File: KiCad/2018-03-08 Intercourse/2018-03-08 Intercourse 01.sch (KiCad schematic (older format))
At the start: 27 parts

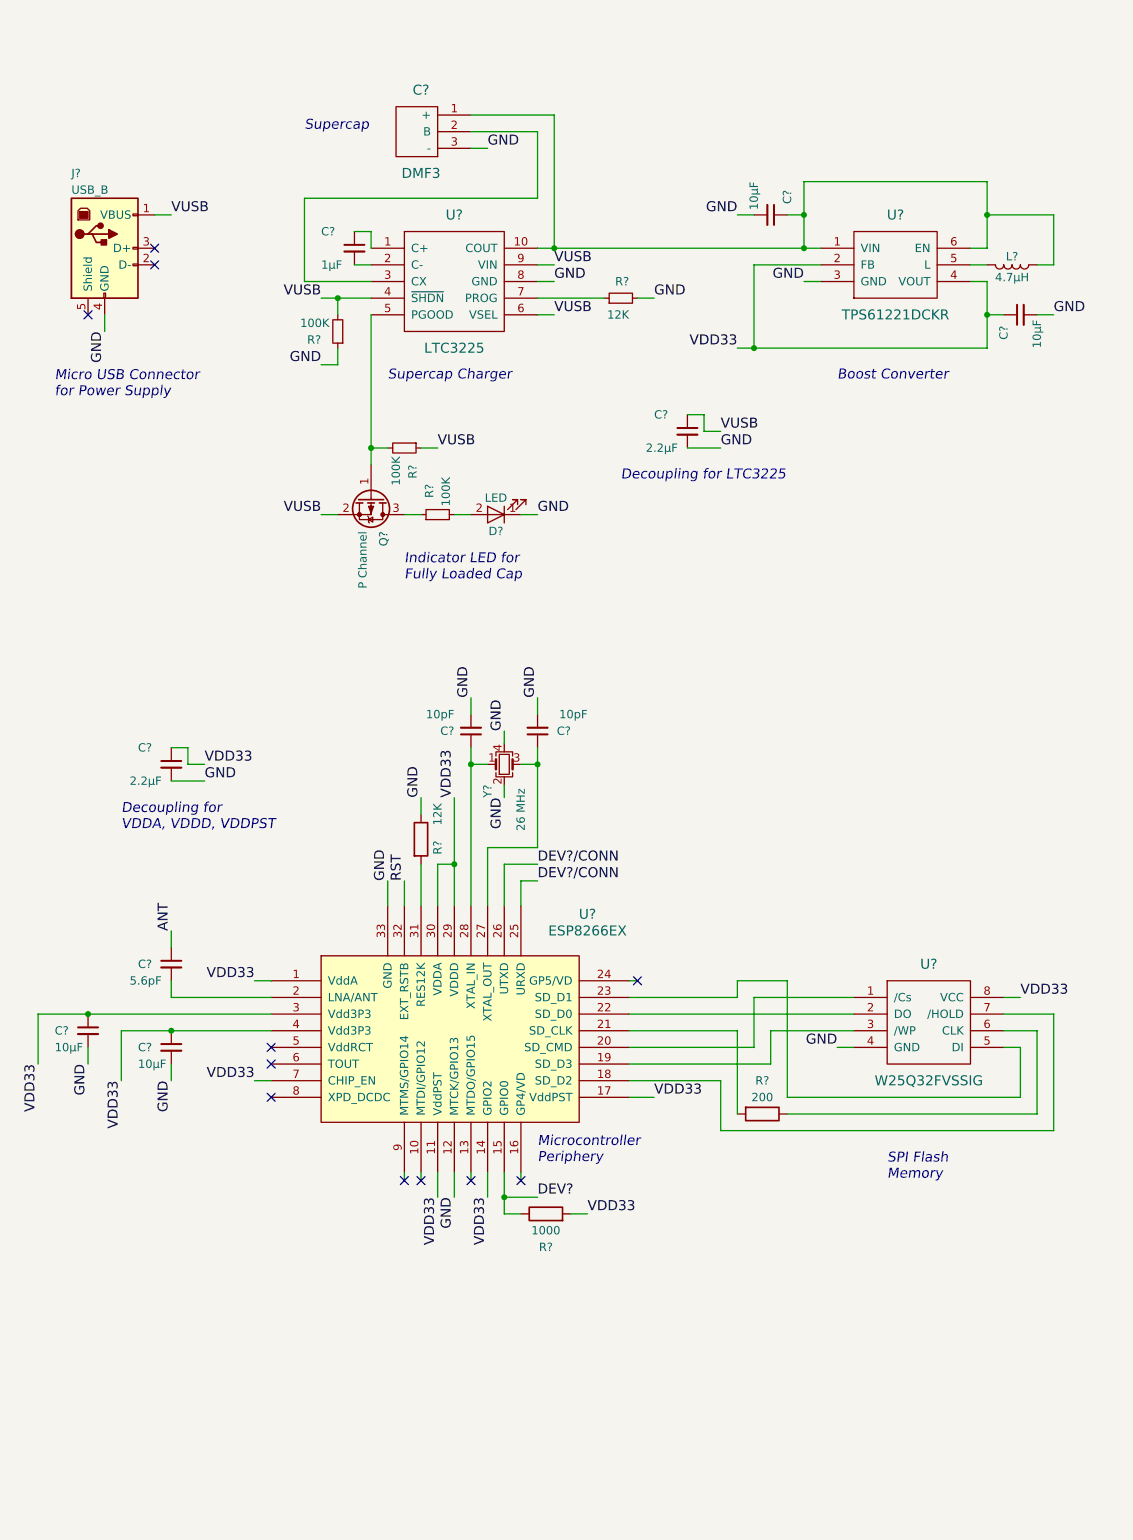
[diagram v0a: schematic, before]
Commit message: clean up schematic
* added connector
* changed labels
* made some stuff cleaner
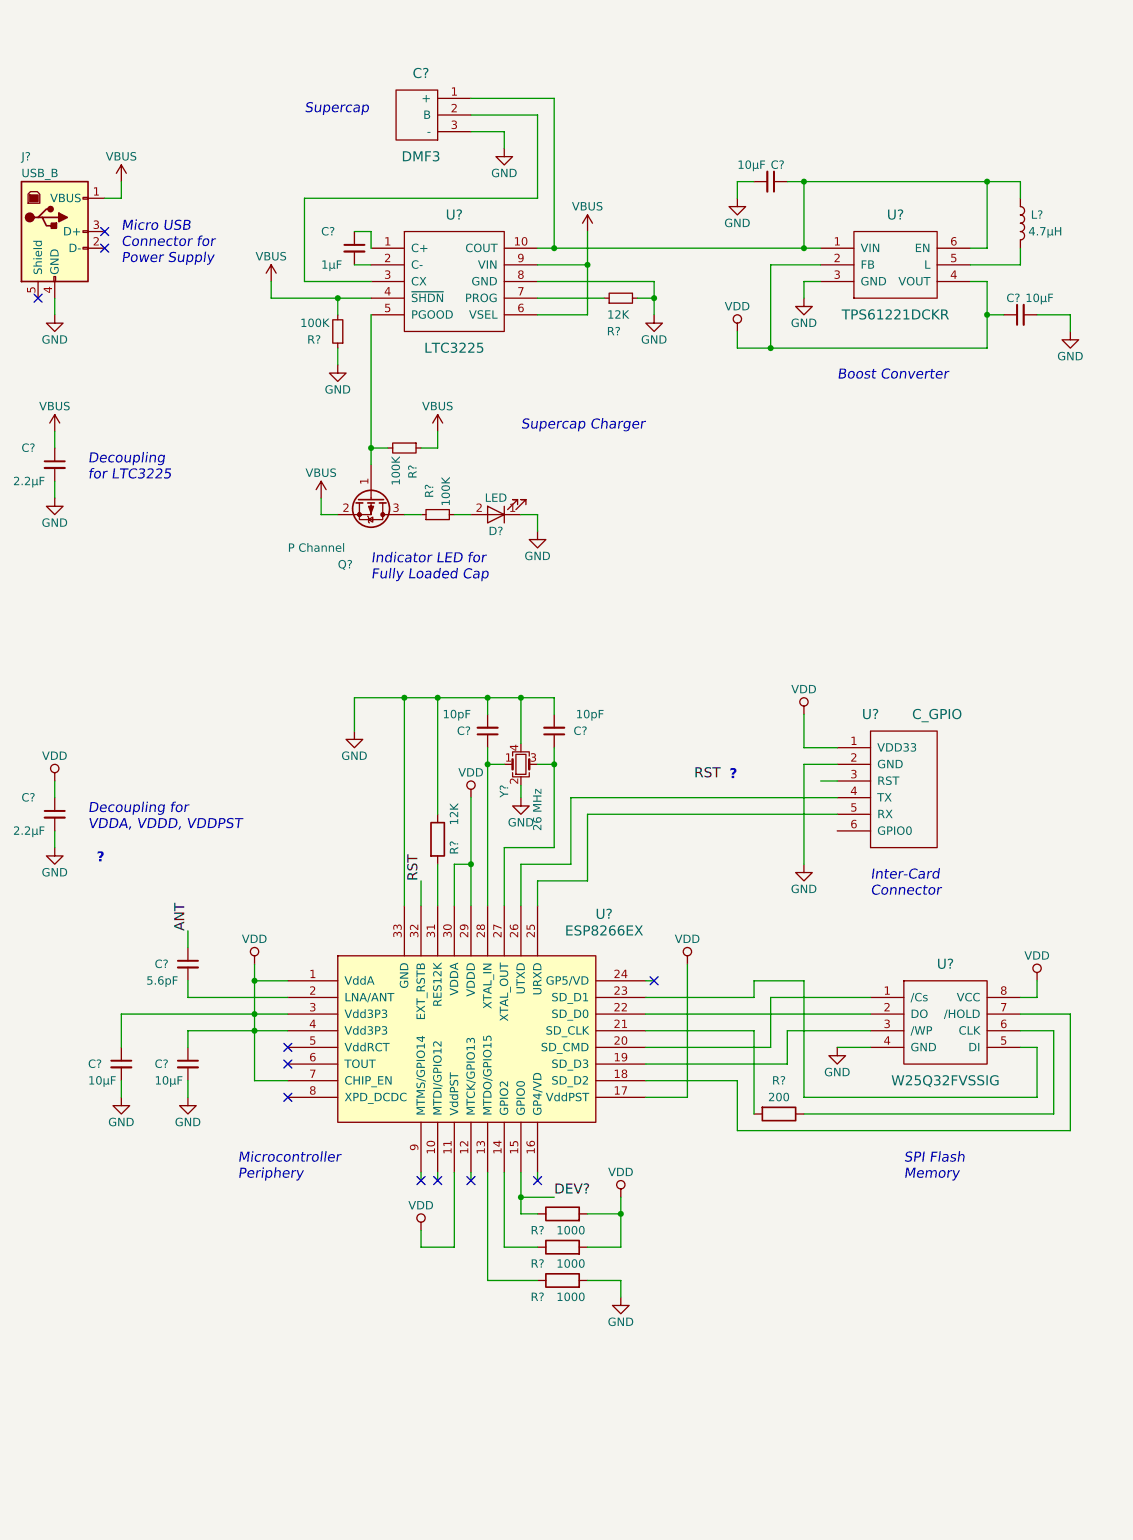
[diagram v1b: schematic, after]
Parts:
- added R? (x2): 1000, symbol R
- added U?: C_GPIO, symbol C_GPIO
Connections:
- net GND: now also R?.2, U?.2 (GND); no longer U?.12 (MTCK/GPIO13)
- net at U?.13 (MTDO/GPIO15): now also R?.1
- net DEV?/CONN: no longer names the net of U?.25 (URXD)
- net DEV?/CONN: now also U?.5 (RX); no longer U?.26 (UTXD)
- net VDD33 renamed VDD
- net VDD: now also R?.2, U?.1 (VDD33); no longer U?.14 (GPIO2)
- net VUSB renamed VBUS
- new net: R?.1, U?.14 (GPIO2)
- new net: U?.26 (UTXD), U?.4 (TX)
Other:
- note added: "?"
- note added: "Decoupling\nfor LTC3225"
- note added: "Inter-Card\nConnector"
- note added: "Micro USB\nConnector for\nPower Supply"
- note removed: "Decoupling for LTC3225"
- note removed: "Micro USB Connector\nfor Power Supply"
- moved on the sheet: C?, J?, L?, R?, U?, Y?

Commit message: further cleaning
* cleaned up
* added todos
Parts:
- added AE?: Antenna, symbol Antenna
- added C?: 1μF, symbol C_Small
- added R?: 10K, symbol R
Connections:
- net DEV? is gone; now on net FLASH: R?.1, U?.15 (GPIO0)
- net RST: now also U?.3 (RST), C?.1, R?.2
- net VDD: now also R?.1
- net FLASH: now reaches U?.6 (GPIO0)
- net ANT: no longer names the net of C?.1
- net ANT: now also AE?.1 (A)
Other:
- note added: "Todo:\n* Status LEDs\n* USB Conn Check\n* Reset"
- moved on the sheet: C?, R?, U?

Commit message: changes labels
Because I like them better ...
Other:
- moved on the sheet: R?
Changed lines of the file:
@@
 L R R?
 U 1 1 5AADBBEB
-P 4150 8200
-F 0 "R?" V 4050 8350 50  0000 C CNN
-F 1 "1000" V 4050 8150 50  0000 C CNN
-F 2 "" V 4080 8200 50  0001 C CNN
-F 3 "" H 4150 8200 50  0001 C CNN
-	1    4150 8200
+P 4150 8300
+F 0 "R?" V 4050 8450 50  0000 C CNN
+F 1 "1000" V 4050 8250 50  0000 C CNN
+F 2 "" V 4080 8300 50  0001 C CNN
+F 3 "" H 4150 8300 50  0001 C CNN
+	1    4150 8300
 	0    -1   -1   0
 $EndComp
-Text Label 4100 8100 0    60   ~ 0
-FLASH
-Text Label 3300 6200 1    60   ~ 0
-RST
 NoConn ~ 2500 7500
 NoConn ~ 2500 7300
@@
 Text Notes 6000 6300 0    60   Italic 0
 Inter-Card\nConnector
-Text Label 5100 5600 2    60   ~ 0
-RST
 $Comp
 L C_GPIO U?
@@
 L R R?
 U 1 1 5AB011DC
-P 4150 8400
-F 0 "R?" V 4050 8550 50  0000 C CNN
-F 1 "1000" V 4050 8350 50  0000 C CNN
-F 2 "" V 4080 8400 50  0001 C CNN
-F 3 "" H 4150 8400 50  0001 C CNN
-	1    4150 8400
+P 4150 8500
+F 0 "R?" V 4050 8650 50  0000 C CNN
+F 1 "1000" V 4050 8450 50  0000 C CNN
+F 2 "" V 4080 8500 50  0001 C CNN
+F 3 "" H 4150 8500 50  0001 C CNN
+	1    4150 8500
 	0    -1   -1   0
 $EndComp
@@
 L R R?
 U 1 1 5AB01E0B
-P 4150 8600
-F 0 "R?" V 4050 8750 50  0000 C CNN
-F 1 "1000" V 4050 8550 50  0000 C CNN
-F 2 "" V 4080 8600 50  0001 C CNN
-F 3 "" H 4150 8600 50  0001 C CNN
-	1    4150 8600
+P 4150 8700
+F 0 "R?" V 4050 8850 50  0000 C CNN
+F 1 "1000" V 4050 8650 50  0000 C CNN
+F 2 "" V 4080 8700 50  0001 C CNN
+F 3 "" H 4150 8700 50  0001 C CNN
+	1    4150 8700
 	0    -1   -1   0
 $EndComp
@@
 L GND #PWR?
 U 1 1 5AB02ABD
-P 4500 8700
-F 0 "#PWR?" H 4500 8450 50  0001 C CNN
-F 1 "GND" H 4500 8550 50  0000 C CNN
-F 2 "" H 4500 8700 50  0001 C CNN
-F 3 "" H 4500 8700 50  0001 C CNN
-	1    4500 8700
+P 4600 8800
+F 0 "#PWR?" H 4600 8550 50  0001 C CNN
+F 1 "GND" H 4600 8650 50  0000 C CNN
+F 2 "" H 4600 8800 50  0001 C CNN
+F 3 "" H 4600 8800 50  0001 C CNN
+	1    4600 8800
 	1    0    0    -1
 $EndComp
@@
 L VDD #PWR?
 U 1 1 5AB10318
-P 4500 8100
-F 0 "#PWR?" H 4500 7950 50  0001 C CNN
-F 1 "VDD" H 4500 8250 50  0000 C CNN
-F 2 "" H 4500 8100 50  0001 C CNN
-F 3 "" H 4500 8100 50  0001 C CNN
-	1    4500 8100
+P 4600 8200
+F 0 "#PWR?" H 4600 8050 50  0001 C CNN
+F 1 "VDD" H 4600 8350 50  0000 C CNN
+F 2 "" H 4600 8200 50  0001 C CNN
+F 3 "" H 4600 8200 50  0001 C CNN
+	1    4600 8200
 	1    0    0    -1
 $EndComp
@@
 	1    0    0    -1
 $EndComp
-Text Label 5500 5900 2    60   ~ 0
-FLASH
 $Comp
 L R R?
@@
 	4100 1400 4100 2300
 Wire Wire Line
-	4000 2300 5700 2300
-Wire Wire Line
-	3000 2700 3000 3600
+	4000 2300 4100 2300
+Wire Wire Line
+	4100 2300 5600 2300
+Wire Wire Line
+	5600 2300 5700 2300
+Wire Wire Line
+	3000 2700 3000 3500
+Wire Wire Line
+	3000 3500 3000 3600
 Wire Wire Line
 	3100 3500 3000 3500
@@
 	5600 1900 5600 2300
 Wire Wire Line
-	5500 1900 6900 1900
+	5500 1900 5600 1900
+Wire Wire Line
+	5600 1900 6700 1900
+Wire Wire Line
+	6700 1900 6900 1900
 Wire Wire Line
 	6700 1900 6700 2300
@@
 	6600 2500 6700 2500
 Wire Wire Line
-	6700 2900 6700 2500
-Wire Wire Line
-	5200 2900 6700 2900
+	6700 2900 6700 2700
+Wire Wire Line
+	6700 2700 6700 2500
+Wire Wire Line
+	5200 2900 5400 2900
+Wire Wire Line
+	5400 2900 6700 2900
 Wire Wire Line
 	5400 2900 5400 2400
@@
 	1500 7400 1500 7500
 Wire Wire Line
-	3200 5000 3200 6350
+	3200 5000 3200 5700
+Wire Wire Line
+	3200 5700 3200 6350
 Wire Wire Line
 	3300 6200 3300 6350
@@
 	3500 7950 3500 8400
 Wire Wire Line
-	3700 7950 3700 8600
-Wire Wire Line
-	3800 7950 3800 8400
-Wire Wire Line
-	3900 7950 3900 8200
+	3700 7950 3700 8700
+Wire Wire Line
+	3800 7950 3800 8500
+Wire Wire Line
+	3900 7950 3900 8100
+Wire Wire Line
+	3900 8100 3900 8300
 Wire Wire Line
 	4000 7950 4000 8000
@@
 	3900 5000 3900 5275
 Wire Wire Line
-	3700 5300 3700 6350
+	3700 5300 3700 5400
+Wire Wire Line
+	3700 5400 3700 6350
 Wire Wire Line
 	4000 5400 4100 5400
 Wire Wire Line
-	4100 5300 4100 6000
+	4100 5300 4100 5400
+Wire Wire Line
+	4100 5400 4100 6000
 Wire Wire Line
 	4100 6000 3800 6000
@@
 Connection ~ 3900 8100
 Wire Wire Line
-	3900 8200 4000 8200
-Wire Wire Line
-	4300 8200 4500 8200
+	3900 8300 4000 8300
+Wire Wire Line
+	4300 8300 4600 8300
 Wire Wire Line
 	4000 6200 4300 6200
@@
 	5600 5500 5800 5500
 Wire Wire Line
-	5100 5600 5800 5600
+	5100 5600 5200 5600
+Wire Wire Line
+	5200 5600 5500 5600
+Wire Wire Line
+	5500 5600 5800 5600
 Wire Wire Line
 	4200 5700 4200 6100
@@
 	4300 5800 4300 6200
 Wire Wire Line
-	3800 8400 4000 8400
-Wire Wire Line
-	4500 8400 4300 8400
-Wire Wire Line
-	3700 8600 4000 8600
-Wire Wire Line
-	4300 8600 4500 8600
-Wire Wire Line
-	4500 8600 4500 8700
+	3800 8500 4000 8500
+Wire Wire Line
+	4600 8500 4300 8500
+Wire Wire Line
+	3700 8700 4000 8700
+Wire Wire Line
+	4300 8700 4600 8700
+Wire Wire Line
+	4600 8700 4600 8800
 Connection ~ 3900 5000
 Connection ~ 3700 5000
@@
 Connection ~ 5600 1900
 Wire Wire Line
-	4700 2500 4700 2700
+	4700 2500 4700 2600
+Wire Wire Line
+	4700 2600 4700 2700
 Connection ~ 4700 2600
 Wire Wire Line
@@
 	1100 3700 1100 3800
 Wire Wire Line
-	5600 5000 5600 5400
+	5600 5000 5600 5100
+Wire Wire Line
+	5600 5100 5600 5400
 Wire Wire Line
 	1100 5700 1100 5600
@@
 	2300 7400 2500 7400
 Wire Wire Line
-	4500 8100 4500 8400
-Connection ~ 4500 8200
+	4600 8200 4600 8300
+Wire Wire Line
+	4600 8300 4600 8500
+Connection ~ 4600 8300
 Wire Wire Line
 	3500 8400 3300 8400
@@
 	1500 2000 1500 1900
 Wire Wire Line
-	2400 2600 3000 2600
+	2400 2600 2800 2600
+Wire Wire Line
+	2800 2600 3000 2600
 Wire Wire Line
 	2400 2600 2400 2500
@@
 Connection ~ 2300 6800
 Wire Wire Line
-	2300 6700 2300 7400
+	2300 6700 2300 6800
+Wire Wire Line
+	2300 6800 2300 7000
+Wire Wire Line
+	2300 7000 2300 7100
+Wire Wire Line
+	2300 7100 2300 7400
 Connection ~ 2300 7100
 Connection ~ 2300 7000
@@
 	1900 7200 1900 7100
 Wire Wire Line
-	1900 7100 2500 7100
-Wire Wire Line
-	1500 7000 2500 7000
+	1900 7100 2300 7100
+Wire Wire Line
+	2300 7100 2500 7100
+Wire Wire Line
+	1500 7000 2300 7000
+Wire Wire Line
+	2300 7000 2500 7000
 Wire Wire Line
 	4000 2400 4300 2400
 Wire Wire Line
-	4300 2200 4300 2700
+	4300 2200 4300 2400
+Wire Wire Line
+	4300 2400 4300 2700
 Connection ~ 4300 2400
 Wire Wire Line
@@
 	3400 5000 3400 5200
 Wire Wire Line
-	5500 5900 5800 5900
+	5100 5900 5800 5900
 Wire Wire Line
 	4500 5000 4500 5100
 Connection ~ 4100 5000
 Wire Wire Line
-	3200 5000 4500 5000
+	3200 5000 3400 5000
+Wire Wire Line
+	3400 5000 3700 5000
+Wire Wire Line
+	3700 5000 3900 5000
+Wire Wire Line
+	3900 5000 4100 5000
+Wire Wire Line
+	4100 5000 4500 5000
 Connection ~ 3400 5000
 Wire Wire Line
@@
 	3500 6200 3600 6200
 Wire Wire Line
-	3600 6000 3600 6350
+	3600 6000 3600 6200
+Wire Wire Line
+	3600 6200 3600 6350
 Connection ~ 3600 6200
 Text Notes 1400 9200 0    60   Italic 12
 Todo:\n* Status LEDs\n* USB Conn Check\n* Reset
+Text GLabel 5100 5900 0    60   Input ~ 0
+FLASH
+Text GLabel 5100 5600 0    60   Input ~ 0
+RST
+Text GLabel 4100 8100 2    60   Input ~ 0
+FLASH
+Text GLabel 3300 6200 1    60   Input ~ 0
+RST
 $EndSCHEMATC
